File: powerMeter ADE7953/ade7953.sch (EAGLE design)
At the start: 44 parts, among them IC1 ADE7953

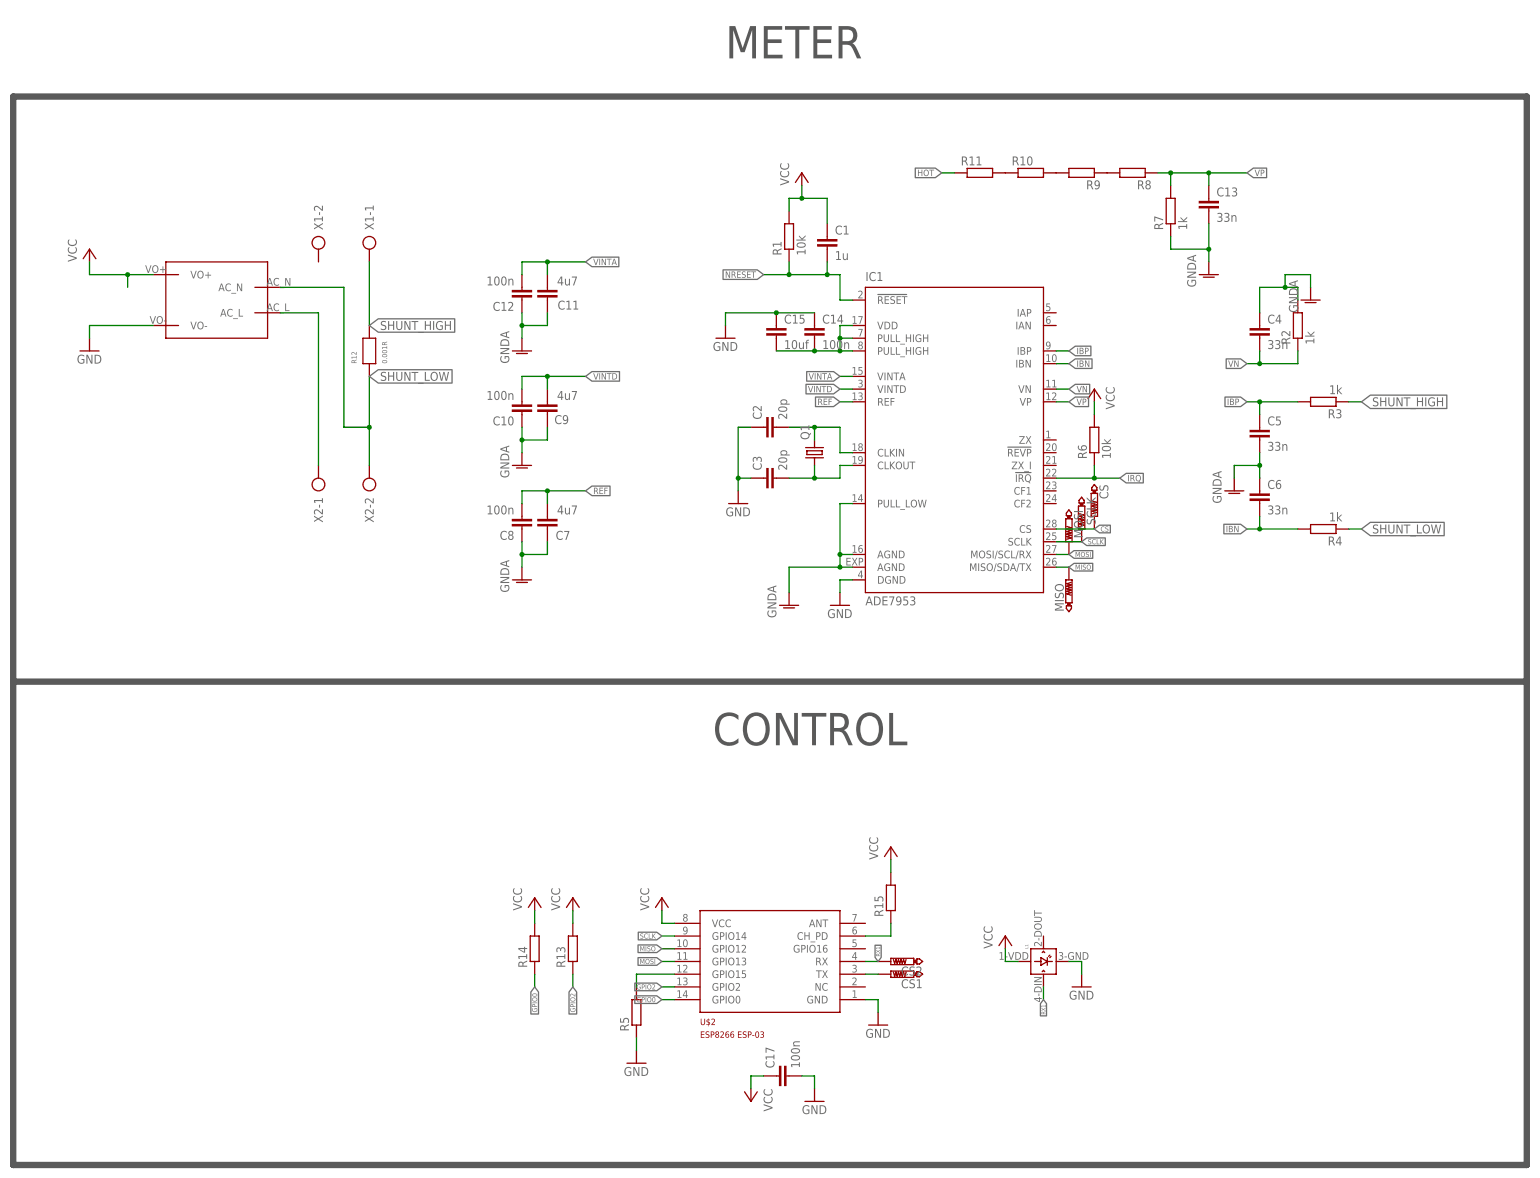
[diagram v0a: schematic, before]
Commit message: updated WiSwitch, tiny433mhz and ade7953
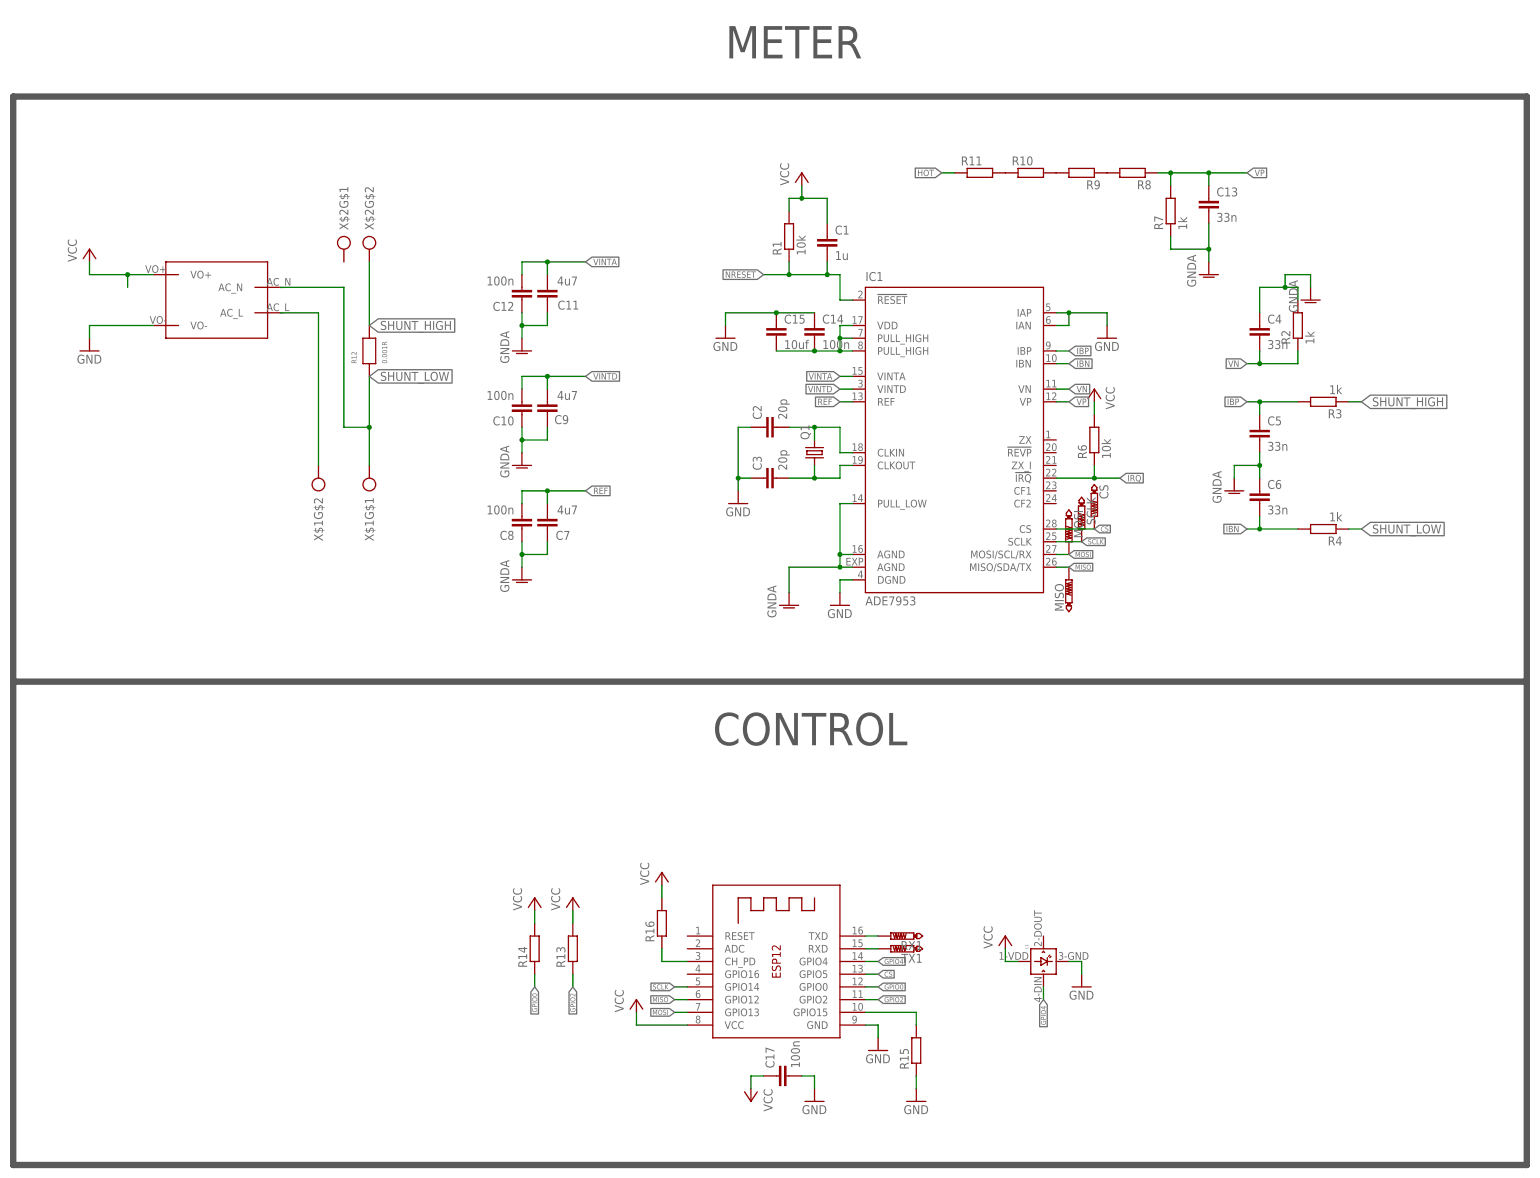
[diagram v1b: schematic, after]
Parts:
- removed CS1, CS2: PTR1B1,27, testpad:PTR1B1,27
- removed R5: (no value), rcl:R-EU_R0603
- removed U$2: ESP8266_ESP-03, ESP8266:ESP8266_ESP-03
- removed X1, X2: (no value), con-ptr500:AK300/2
- added R16: (no value), rcl:R-EU_R0603
- added RX1, TX1: PTR1B1,27, testpad:PTR1B1,27
- added X$1, X$2: ARK2, _ARK:ARK2
- added X3: (no value), adafruit:ESP-12
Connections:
- removed net N$3: R15.1, U$2.CH_PD
- removed net RX1: CS2.TP, L1.DIN, U$2.RX
- removed net TX1: CS1.TP, U$2.TX
- new net GPIO15: R15.2, X3.GPIO15
- new net GPIO4: L1.DIN, X3.GPIO4
- new net N$4: R16.1, X3.CH_PD
- new net RX: TX1.TP, X3.RXD
- new net TX: RX1.TP, X3.TXD
- net CS: now also X3.GPIO5; no longer R5.2, U$2.GPIO15
- net GND: now also IC1.IAN, IC1.IAP, R15.1, X3.GND; no longer R5.1, U$2.GND
- net GPIO0: now also X3.GPIO0; no longer U$2.GPIO0
- net GPIO2: now also X3.GPIO2; no longer U$2.GPIO2
- net HOT: now also X$1G$2.KL; no longer X2-1.KL
- net MISO: now also X3.GPIO12; no longer U$2.GPIO12
- net MOSI: now also X3.GPIO13; no longer U$2.GPIO13
- net SCLK: now also X3.GPIO14; no longer U$2.GPIO14
- net SHUNT_HIGH: now also X$2G$2.KL; no longer X1-1.KL
- net SHUNT_LOW: now also X$1G$1.KL; no longer X2-2.KL
- net VCC: now also R16.2, X3.VCC; no longer R15.2, U$2.VCC
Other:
- moved on the sheet: R15
